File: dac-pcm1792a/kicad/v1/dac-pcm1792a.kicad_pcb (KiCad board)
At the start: 2 copper layers, 76.2 x 53.3 mm, 81 parts, among them IC1 PCM1702P, IC2 PCM1702P, J10 GND, J11 +15VAIN, J12 GND, J13 -15VAIN, J15 A, J16 +5VIN, J17 GND, J18 GND, J2 Conn_02x07_Odd_Even, J3 +5VAIN, J6 OUT, J7 -5VAIN, J8 GND, J9 OUT, U1 OPA1612, U2 TC1185-1.8VCT713, U3 TC1185-3.3VCT713, U4 XC2C64A-xVQ44, U5 CM1293A−04SO, U6 OPA1612

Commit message: WIP
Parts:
- removed C25: 10uF/10V, Capacitor_Tantalum_SMD:CP_EIA-3216-18_Kemet-A_Pad1.58x1.35mm_HandSolder
- removed C26: 100nF, Capacitor_SMD:C_0603_1608Metric_Pad1.08x0.95mm_HandSolder
- removed C27, C28, C29, C30: 10uF/25V, Capacitor_Tantalum_SMD:CP_EIA-3216-18_Kemet-A_Pad1.58x1.35mm_HandSolder
- removed C31, C42: 2n2, Capacitor_SMD:C_0805_2012Metric_Pad1.18x1.45mm_HandSolder
- removed C32, C43: 560p, Capacitor_SMD:C_0805_2012Metric_Pad1.18x1.45mm_HandSolder
- removed C41: 220pF, Capacitor_SMD:C_0805_2012Metric_Pad1.18x1.45mm_HandSolder
- removed IC1, IC2: PCM1702P, Package_DIP:DIP-16_W7.62mm
- removed J12, J8: GND, Connector_Pin:Pin_D1.0mm_L10.0mm
- removed J6: OUT, Connector_Pin:Pin_D1.0mm_L10.0mm
- removed J7: -5VAIN, Connector_Pin:Pin_D1.0mm_L10.0mm
- removed U1: OPA1612, Package_SO:SOIC-8_3.9x4.9mm_P1.27mm
- added J1: PORTB, Connector_PinHeader_2.54mm:PinHeader_1x08_P2.54mm_Vertical, F.Cu at (119.4, 97.8)
- added J4: GND, Connector_Pin:Pin_D1.0mm_L10.0mm, F.Cu at (161.3, 50.0)
- added J5: +5VAGND, Connector_Pin:Pin_D1.0mm_L10.0mm, F.Cu at (147.3, 111.1)
- added R1: 4k7, Resistor_SMD:R_0603_1608Metric_Pad0.98x0.95mm_HandSolder, F.Cu at (157.1, 49.8)
- added R12: 560R/0.1%, Resistor_SMD:R_0603_1608Metric_Pad0.98x0.95mm_HandSolder, F.Cu at (156.7, 83.8)
- added R13: 560R/0.1%, Resistor_SMD:R_0603_1608Metric_Pad0.98x0.95mm_HandSolder, F.Cu at (156.7, 81.3)
- added R14: 270R/0.1%, Resistor_SMD:R_0603_1608Metric_Pad0.98x0.95mm_HandSolder, F.Cu at (122.7, 34.9)
- added R15: 270R/0.1%, Resistor_SMD:R_0603_1608Metric_Pad0.98x0.95mm_HandSolder, F.Cu at (127.5, 31.9)
- added R16: 270R/0.1%, Resistor_SMD:R_0603_1608Metric_Pad0.98x0.95mm_HandSolder, F.Cu at (122.7, 37.4)
- added R17: 270R/0.1%, Resistor_SMD:R_0603_1608Metric_Pad0.98x0.95mm_HandSolder, F.Cu at (127.0, 34.9)
- added R18: 100R/0.1%, Resistor_SMD:R_0603_1608Metric_Pad0.98x0.95mm_HandSolder, F.Cu at (147.8, 52.9)
- added R19: 100R/0.1%, Resistor_SMD:R_0603_1608Metric_Pad0.98x0.95mm_HandSolder, F.Cu at (152.6, 50.0)
- added R2: 10k, Resistor_SMD:R_0603_1608Metric_Pad0.98x0.95mm_HandSolder, F.Cu at (150.3, 55.7)
- added R3: 33R, Resistor_SMD:R_0603_1608Metric_Pad0.98x0.95mm_HandSolder, F.Cu at (164.4, 42.4)
- C1: value 220pF -> 10uF/10V; footprint Capacitor_SMD:C_0805_2012Metric_Pad1.18x1.45mm_HandSolder -> Capacitor_Tantalum_SMD:CP_EIA-3216-18_Kemet-A_Pad1.58x1.35mm_HandSolder; moved to B.Cu
- C10: value 100uF -> 10uF/10V; footprint Capacitor_SMD:C_1206_3216Metric_Pad1.33x1.80mm_HandSolder -> Capacitor_Tantalum_SMD:CP_EIA-3216-18_Kemet-A_Pad1.58x1.35mm_HandSolder; moved to B.Cu
- C11, C12: value 100uF -> 47uF/10V; footprint Capacitor_SMD:C_1206_3216Metric_Pad1.33x1.80mm_HandSolder -> Capacitor_Tantalum_SMD:CP_EIA-3528-12_Kemet-T_Pad1.50x2.35mm_HandSolder; moved to B.Cu
- C13, C14, C15: value 100nF -> 2200pF/2%; footprint Capacitor_SMD:C_0603_1608Metric_Pad1.08x0.95mm_HandSolder -> Capacitor_SMD:C_0805_2012Metric_Pad1.18x1.45mm_HandSolder
- C16: value 10uF/25V -> 2200pF/2%; footprint Capacitor_Tantalum_SMD:CP_EIA-3216-18_Kemet-A_Pad1.58x1.35mm_HandSolder -> Capacitor_SMD:C_0805_2012Metric_Pad1.18x1.45mm_HandSolder
- C17: value 10uF/25V -> 2700pF/2%; footprint Capacitor_Tantalum_SMD:CP_EIA-3216-18_Kemet-A_Pad1.58x1.35mm_HandSolder -> Capacitor_SMD:C_0805_2012Metric_Pad1.18x1.45mm_HandSolder
- C18: value 10uF/10V -> 2700pF/2%; footprint Capacitor_Tantalum_SMD:CP_EIA-3216-18_Kemet-A_Pad1.58x1.35mm_HandSolder -> Capacitor_SMD:C_0805_2012Metric_Pad1.18x1.45mm_HandSolder
- C19, C20: value 100uF -> 2700pF/2%; footprint Capacitor_SMD:C_1206_3216Metric_Pad1.33x1.80mm_HandSolder -> Capacitor_SMD:C_0805_2012Metric_Pad1.18x1.45mm_HandSolder
- C21: value 100uF -> 10uF/25V; footprint Capacitor_SMD:C_1206_3216Metric_Pad1.33x1.80mm_HandSolder -> Capacitor_Tantalum_SMD:CP_EIA-3528-21_Kemet-B_Pad1.50x2.35mm_HandSolder
- C22: value 100nF -> 10uF/25V; footprint Capacitor_SMD:C_0603_1608Metric_Pad1.08x0.95mm_HandSolder -> Capacitor_Tantalum_SMD:CP_EIA-3528-21_Kemet-B_Pad1.50x2.35mm_HandSolder
- C3: value 10uF -> 10uF/10V; footprint Capacitor_SMD:C_0805_2012Metric_Pad1.18x1.45mm_HandSolder -> Capacitor_Tantalum_SMD:CP_EIA-3216-18_Kemet-A_Pad1.58x1.35mm_HandSolder; moved to B.Cu
- C8: moved to B.Cu
- C9: value 100nF -> 10uF/10V; footprint Capacitor_SMD:C_0603_1608Metric_Pad1.08x0.95mm_HandSolder -> Capacitor_Tantalum_SMD:CP_EIA-3216-18_Kemet-A_Pad1.58x1.35mm_HandSolder
- J2: value Conn_02x07_Odd_Even -> OUT; footprint Connector_PinHeader_2.00mm:PinHeader_2x07_P2.00mm_Vertical -> Connector_Pin:Pin_D1.0mm_L10.0mm
- R10: value 4.7k -> 560R/0.1%; footprint Resistor_SMD:R_0805_2012Metric_Pad1.20x1.40mm_HandSolder -> Resistor_SMD:R_0603_1608Metric_Pad0.98x0.95mm_HandSolder
- R11: value 2k -> 560R/0.1%; footprint Resistor_SMD:R_0805_2012Metric_Pad1.20x1.40mm_HandSolder -> Resistor_SMD:R_0603_1608Metric_Pad0.98x0.95mm_HandSolder
- R4: value 2.5k -> 33R; footprint Resistor_SMD:R_0805_2012Metric_Pad1.20x1.40mm_HandSolder -> Resistor_SMD:R_0603_1608Metric_Pad0.98x0.95mm_HandSolder
- R5: value 4.7k -> 33R; footprint Resistor_SMD:R_0805_2012Metric_Pad1.20x1.40mm_HandSolder -> Resistor_SMD:R_0603_1608Metric_Pad0.98x0.95mm_HandSolder
- R6, R9: value 4.7k -> 750R/0.1%; footprint Resistor_SMD:R_0805_2012Metric_Pad1.20x1.40mm_HandSolder -> Resistor_SMD:R_0603_1608Metric_Pad0.98x0.95mm_HandSolder
- R7: value 2k -> 750R/0.1%; footprint Resistor_SMD:R_0805_2012Metric_Pad1.20x1.40mm_HandSolder -> Resistor_SMD:R_0603_1608Metric_Pad0.98x0.95mm_HandSolder
- R8: value 2.5k -> 750R/0.1%; footprint Resistor_SMD:R_0805_2012Metric_Pad1.20x1.40mm_HandSolder -> Resistor_SMD:R_0603_1608Metric_Pad0.98x0.95mm_HandSolder
- U2: value TC1185-1.8VCT713 -> PCM1792A; footprint Package_TO_SOT_SMD:SOT-23-5 -> Package_SO:SSOP-28_5.3x10.2mm_P0.65mm
- U4: value XC2C64A-xVQ44 -> OPA1612; footprint Package_QFP:TQFP-44_10x10mm_P0.8mm -> Package_SO:SOIC-8_3.9x4.9mm_P1.27mm
- U5: value CM1293A−04SO -> OPA1612; footprint Package_SO:SC-74-6_1.5x2.9mm_P0.95mm -> Package_SO:SOIC-8_3.9x4.9mm_P1.27mm
- moved C19 79.1 mm to (122.9, 32.1)
- moved C20 67.4 mm to (118.1, 38.1)
- moved U5 67.1 mm to (174.6, 54.0)
- moved J2 55.1 mm to (154.5, 56.0)
- moved C17 50.1 mm to (118.1, 32.1), turned to 0 degrees
- moved C13 41.8 mm to (151.6, 107.5), turned to 0 degrees
- moved C18 41.2 mm to (118.1, 35.1), turned to 0 degrees
- moved R6 36.2 mm to (151.5, 105.5), turned to 0 degrees
- moved R7 31.0 mm to (152.1, 95.6), turned to 0 degrees
- moved C37 30.7 mm to (146.4, 76.1)
- moved C1 30.5 mm to (137.2, 83.8), turned to 180 degrees
- moved U4 29.3 mm to (152.4, 100.3)
- moved C12 28.6 mm to (137.2, 88.9)
- moved R5 27.9 mm to (163.0, 44.9), turned to 0 degrees
- moved C14 25.3 mm to (152.1, 93.8), turned to 0 degrees
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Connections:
- C1 pad 1: Net-(C1-Pad1) -> +5VA
- C1 pad 2: Net-(C1-Pad2) -> GND
- C10 pad 1: Net-(C10-Pad1) -> +5VA
- C11 pad 1: Net-(C11-Pad1) -> +5VA
- C11 pad 2: -5VA -> Net-(C11-Pad2)
- C12 pad 1: Net-(C12-Pad1) -> +5VA
- C12 pad 2: -5VA -> Net-(C12-Pad2)
- C13 pad 1: -5VA -> Net-(C13-Pad1)
- C13 pad 2: GND -> Net-(C13-Pad2)
- C14 pad 1: +5VA -> Net-(C14-Pad1)
- C14 pad 2: GND -> Net-(C14-Pad2)
- C15 pad 1: -5VA -> Net-(C15-Pad1)
- C15 pad 2: GND -> Net-(C15-Pad2)
- C16 pad 1: +5VA -> Net-(C16-Pad1)
- C16 pad 2: GND -> Net-(C16-Pad2)
- C17 pad 2: -5VA -> Net-(C17-Pad2)
- C18 pad 1: +5VA -> Net-(C18-Pad1)
- C18 pad 2: GND -> Net-(C18-Pad2)
- C19 pad 1: Net-(C19-Pad1) -> GND
- C19 pad 2: GND -> Net-(C19-Pad2)
- C20 pad 2: -5VA -> Net-(C20-Pad2)
- C21 pad 1: Net-(C21-Pad1) -> +15V
- C21 pad 2: -5VA -> GND
- C22 pad 1: -5VA -> GND
- C22 pad 2: GND -> -15V
- C23 pad 1: +5VA -> +15V
- C24 pad 1: -5VA -> GND
- C24 pad 2: GND -> -15V
- C3 pad 1: +1V8 -> +3V3
- C5 pad 1: GND -> +5VA
- C5 pad 2: +3V3 -> GND
- C6 pad 1: GND -> +3V3
- C6 pad 2: +3V3 -> GND
- C7 pad 1: GND -> +5VA
- C7 pad 2: +1V8 -> GND
- C8 pad 1: GND -> +5VA
- C8 pad 2: +3V3 -> GND
- J15 pad 10: (no net) -> Net-(J1-Pad7)
- J15 pad 6: (no net) -> Net-(J1-Pad5)
- J15 pad 8: (no net) -> Net-(J1-Pad6)
- J2 pad 1: GND -> Net-(J2-Pad1)
- J9 pad 1: Net-(C43-Pad1) -> Net-(J9-Pad1)
- R10 pad 1: Net-(C31-Pad1) -> Net-(C17-Pad2)
- R10 pad 2: Net-(C32-Pad1) -> Net-(C13-Pad1)
- R11 pad 1: Net-(C32-Pad2) -> Net-(C18-Pad1)
- R11 pad 2: Net-(C31-Pad1) -> Net-(C14-Pad1)
- R4 pad 1: Net-(C41-Pad2) -> SCL
- R4 pad 2: Net-(C41-Pad1) -> Net-(J1-Pad6)
- R5 pad 1: Net-(C42-Pad1) -> SDA
- R5 pad 2: Net-(C41-Pad2) -> Net-(J1-Pad5)
- R6 pad 1: Net-(C42-Pad1) -> Net-(C13-Pad1)
- R6 pad 2: Net-(C43-Pad1) -> Net-(C13-Pad2)
- R7 pad 1: Net-(C43-Pad2) -> Net-(C14-Pad1)
- R7 pad 2: Net-(C42-Pad1) -> Net-(C14-Pad2)
- R8 pad 1: Net-(C1-Pad2) -> Net-(C15-Pad1)
- R8 pad 2: Net-(C1-Pad1) -> Net-(C15-Pad2)
- R9 pad 1: Net-(C31-Pad1) -> Net-(C16-Pad1)
- R9 pad 2: Net-(C1-Pad2) -> Net-(C16-Pad2)
- U2 pad 1: Net-(C2-Pad1) -> (no net)
- U2 pad 2: GND -> (no net)
- U2 pad 3: Net-(C2-Pad1) -> Net-(R1-Pad2)
- U2 pad 4: (no net) -> LRCK
- U2 pad 5: +1V8 -> DATAIN
- U4 pad 1: (no net) -> Net-(C13-Pad1)
- U4 pad 2: (no net) -> Net-(C13-Pad2)
- U4 pad 3: (no net) -> GND
- U4 pad 4: GND -> -15V
- U4 pad 5: (no net) -> GND
- U4 pad 6: (no net) -> Net-(C14-Pad2)
- U4 pad 7: +3V3 -> Net-(C14-Pad1)
- U4 pad 8: (no net) -> +15V
- U5 pad 1: JTAG_TMS -> Net-(C20-Pad2)
- U5 pad 2: GND -> Net-(C20-Pad1)
- U5 pad 3: JTAG_TDO -> Net-(C19-Pad2)
- U5 pad 4: JTAG_TCK -> -15V
- U5 pad 5: +3V3 -> Net-(C17-Pad2)
- U5 pad 6: JTAG_TDI -> Net-(C18-Pad1)
- U6 pad 1: Net-(C41-Pad2) -> Net-(C15-Pad1)
- U6 pad 2: Net-(C41-Pad1) -> Net-(C15-Pad2)
- U6 pad 6: Net-(C43-Pad2) -> Net-(C16-Pad2)
- U6 pad 7: Net-(C43-Pad1) -> Net-(C16-Pad1)
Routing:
- net -5VA: track 105.7 -> 0.00 mm, vias 3 -> 0
- net +5VA: track 77.8 -> 0.00 mm, vias 3 -> 0
- net +3V3: track 74.6 -> 0.01 mm, vias 5 -> 0
- net +15V: track 45.2 -> 0.00 mm, vias 2 -> 0
- net JTAG_TDO: track 44.7 -> 0.00 mm, vias 4 -> 0
- net -15V: track 41.9 -> 0.00 mm, vias 2 -> 0
- net JTAG_TDI: track 33.7 -> 0.00 mm, vias 6 -> 0
- net JTAG_TCK: track 32.0 -> 0.00 mm, vias 4 -> 0
- net +1V8: track 29.6 -> 0.00 mm, vias 2 -> 0
- net JTAG_TMS: track 28.1 -> 0.00 mm, vias 4 -> 0
- net Net-(C2-Pad1): track 22.5 -> 0.00 mm, vias 3 -> 0
- net LEOUTL: track 21.8 -> 0.00 mm, vias 1 -> 0
- net Net-(C32-Pad1): track 16.9 -> 0.00 mm, vias 2 -> 0
- net Net-(C43-Pad1): track 16.7 -> 0.00 mm, vias 2 -> 0
- net DATAOUTR: track 16.0 -> 0.00 mm, vias 1 -> 0
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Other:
- board text added: "DAC PCM1792A V1 Michael Schenk 2021.06.06"
- board text removed: "-5VA"
- board text removed: "I2S NOS CPLD V4 Michael Schenk 2021.05.14"
- board text removed: "JTAG"

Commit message: WIP
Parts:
- C3: moved to F.Cu
- moved R3 55.7 mm to (123.3, 80.1), turned to 180 degrees
- moved R5 55.1 mm to (123.3, 83.2), turned to 180 degrees
- moved R4 35.8 mm to (123.3, 81.7), turned to 180 degrees
- moved U5 31.5 mm to (173.5, 85.5)
- moved R24 13.0 mm to (123.3, 97.8)
- moved R25 12.1 mm to (123.3, 95.2)
- moved R26 11.2 mm to (123.3, 92.7)
- moved R27 10.3 mm to (123.3, 90.2)
- moved R12 8.46 mm to (158.6, 75.5)
- moved R13 8.46 mm to (158.6, 73.1)
- moved C16 8.46 mm to (153.6, 67.9)
- moved C38 8.46 mm to (159.2, 79.5)
- moved R8 8.46 mm to (152.2, 78.8)
- moved R9 8.46 mm to (153.6, 69.8)
- moved U6 8.46 mm to (153.6, 74.3)
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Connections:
- J1 pad 1: (no net) -> Net-(J1-Pad1)
- J1 pad 2: (no net) -> Net-(J1-Pad2)
- J1 pad 3: (no net) -> Net-(J1-Pad3)
- J1 pad 4: (no net) -> Net-(J1-Pad4)
- J15 pad 1: Net-(J15-Pad1) -> Net-(J1-Pad1)
- J15 pad 3: Net-(J15-Pad3) -> Net-(J1-Pad2)
- J15 pad 5: Net-(J15-Pad5) -> Net-(J1-Pad3)
- J15 pad 7: Net-(J15-Pad7) -> Net-(J1-Pad4)
- R24 pad 1: Net-(J15-Pad1) -> Net-(J1-Pad1)
- R25 pad 1: Net-(J15-Pad3) -> Net-(J1-Pad2)
- R26 pad 1: Net-(J15-Pad5) -> Net-(J1-Pad3)
- R27 pad 1: Net-(J15-Pad7) -> Net-(J1-Pad4)
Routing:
- net Net-(J1-Pad1): track 0.00 -> 8.32 mm
- net Net-(J1-Pad3): track 0.00 -> 8.32 mm
- net Net-(J1-Pad2): track 0.00 -> 8.32 mm
- net Net-(J1-Pad4): track 0.00 -> 8.26 mm
- net Net-(J1-Pad7): track 0.00 -> 6.76 mm
- net Net-(J1-Pad5): track 0.00 -> 6.76 mm
- net Net-(J1-Pad6): track 0.00 -> 6.76 mm
- net SDA: track 0.00 -> 1.83 mm, vias 0 -> 1
- net +5VA: track 0.00 -> 1.56 mm, vias 0 -> 1
- net RESET: track 0.00 -> 1.45 mm, vias 0 -> 1
- net SCL: track 0.00 -> 1.34 mm, vias 0 -> 1
- net LRCK: track 0.54 -> 0.00 mm

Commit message: Update dac-pcm1792a.kicad_pcb
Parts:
- moved C6 1.27 mm to (130.9, 88.8), turned to 270 degrees
- moved C3 1.01 mm to (129.0, 89.4), turned to 270 degrees
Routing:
- net RESET: track 1.45 -> 22.2 mm, vias 1 -> 2
- net SCL: track 1.34 -> 18.9 mm, vias 1 -> 2
- net SDA: track 1.83 -> 18.0 mm, vias 1 -> 2
- net LRCK: track 0.00 -> 13.5 mm, vias 0 -> 2
- net DATAIN: track 0.00 -> 10.7 mm, vias 0 -> 2
- net GND: track 1.20 -> 9.52 mm
- net Net-(J1-Pad5): track 6.76 -> 12.6 mm, vias 0 -> 1
- net Net-(J1-Pad6): track 6.76 -> 12.0 mm, vias 0 -> 1
- net Net-(J1-Pad7): track 6.76 -> 11.0 mm, vias 0 -> 1
- net +3V3: track 0.01 -> 3.91 mm, vias 0 -> 1
- net MCLK: track 0.00 -> 1.84 mm, vias 0 -> 1
- net BCK: track 0.00 -> 1.43 mm, vias 0 -> 1

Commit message: WIP
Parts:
- moved R1 43.1 mm to (129.9, 83.1), turned to 270 degrees
- moved C2 5.55 mm to (131.2, 106.1), turned to 0 degrees
- moved U3 4.80 mm to (131.1, 103.0)
- moved R24 4.70 mm to (123.3, 93.1)
- moved R25 4.32 mm to (123.3, 90.9)
- moved C4 4.18 mm to (131.2, 100.0)
- moved R26 3.30 mm to (123.3, 89.4)
- moved R27 2.86 mm to (123.3, 87.3)
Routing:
- net +3V3: track 3.91 -> 17.9 mm, vias 1 -> 2
- net Net-(C2-Pad1): track 0.00 -> 11.5 mm, vias 0 -> 1
- net MCLK: track 1.84 -> 12.0 mm, vias 1 -> 2
- net BCK: track 1.43 -> 10.8 mm, vias 1 -> 2
- net Net-(J1-Pad1): track 8.32 -> 5.27 mm
- net Net-(J1-Pad3): track 8.32 -> 5.27 mm
- net Net-(J1-Pad2): track 8.32 -> 5.27 mm
- net Net-(J1-Pad4): track 8.26 -> 5.27 mm
- net LRCK: track 13.5 -> 11.9 mm
- net GND: track 9.52 -> 10.7 mm
- net DATAIN: track 10.7 -> 9.56 mm

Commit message: WIP
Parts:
- C10, C8: moved to F.Cu
- moved C18 78.0 mm to (168.6, 94.6)
- moved C17 75.8 mm to (164.7, 91.8), turned to 90 degrees
- moved R15 73.5 mm to (168.6, 92.8)
- moved R14 69.6 mm to (162.9, 91.7), turned to 90 degrees
- moved C20 69.2 mm to (171.4, 82.4)
- moved C19 65.9 mm to (168.9, 79.4), turned to 270 degrees
- moved R17 63.4 mm to (172.3, 79.2)
- moved R16 61.0 mm to (166.9, 79.3), turned to 270 degrees
- moved J4 50.9 mm to (181.4, 96.8)
- moved R18 45.1 mm to (174.7, 89.2), turned to 180 degrees
- moved J2 43.9 mm to (181.4, 90.7)
- moved R19 43.4 mm to (174.7, 87.4), turned to 180 degrees
- moved R2 33.1 mm to (143.1, 87.9), turned to 180 degrees
- moved J3 17.7 mm to (136.2, 111.5)
- moved C36 17.7 mm to (162.4, 84.2), turned to 270 degrees
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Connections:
- U4 pad 1: Net-(C13-Pad1) -> Net-(C14-Pad1)
- U4 pad 2: Net-(C13-Pad2) -> Net-(C14-Pad2)
- U4 pad 6: Net-(C14-Pad2) -> Net-(C13-Pad2)
- U4 pad 7: Net-(C14-Pad1) -> Net-(C13-Pad1)
- U6 pad 1: Net-(C15-Pad1) -> Net-(C16-Pad1)
- U6 pad 2: Net-(C15-Pad2) -> Net-(C16-Pad2)
- U6 pad 6: Net-(C16-Pad2) -> Net-(C15-Pad2)
- U6 pad 7: Net-(C16-Pad1) -> Net-(C15-Pad1)
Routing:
- net +5VA: track 1.56 -> 61.2 mm, vias 1 -> 4
- net -15V: track 0.00 -> 34.4 mm, vias 0 -> 3
- net +15V: track 0.00 -> 32.8 mm, vias 0 -> 2
- net GND: track 10.7 -> 32.9 mm, vias 0 -> 1
- net Net-(C15-Pad2): track 0.00 -> 20.8 mm, vias 0 -> 2
- net Net-(C14-Pad2): track 0.00 -> 20.7 mm, vias 0 -> 2
- net Net-(C13-Pad2): track 0.00 -> 20.2 mm, vias 0 -> 2
- net Net-(C16-Pad2): track 0.00 -> 18.3 mm, vias 0 -> 2
- net Net-(C14-Pad1): track 0.00 -> 11.0 mm
- net Net-(C16-Pad1): track 0.00 -> 11.0 mm
- net +3V3: track 17.9 -> 7.10 mm
- net Net-(C13-Pad1): track 0.00 -> 10.3 mm
- net Net-(C18-Pad2): track 0.00 -> 9.85 mm
- net Net-(C15-Pad1): track 0.00 -> 9.85 mm
- net Net-(C12-Pad2): track 0.00 -> 4.51 mm, vias 0 -> 1
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
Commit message: WIP
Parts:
- moved R17 5.09 mm to (170.1, 83.8)
- moved R16 3.87 mm to (165.2, 82.8)
- moved C19 3.76 mm to (167.1, 82.7)
- moved C34 1.75 mm to (165.0, 86.8), turned to 90 degrees
- moved C20 1.24 mm to (170.2, 82.0)
- moved C18 0.38 mm to (168.9, 94.6)
- moved R15 0.23 mm to (168.8, 92.8)
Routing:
- net Net-(C20-Pad1): track 0.00 -> 17.0 mm, vias 0 -> 2
- net Net-(C19-Pad2): track 0.00 -> 14.1 mm, vias 0 -> 2
- net Net-(C17-Pad2): track 0.00 -> 11.2 mm, vias 0 -> 2
- net Net-(C18-Pad1): track 3.97 -> 14.4 mm, vias 0 -> 2
- net Net-(C20-Pad2): track 4.00 -> 8.20 mm

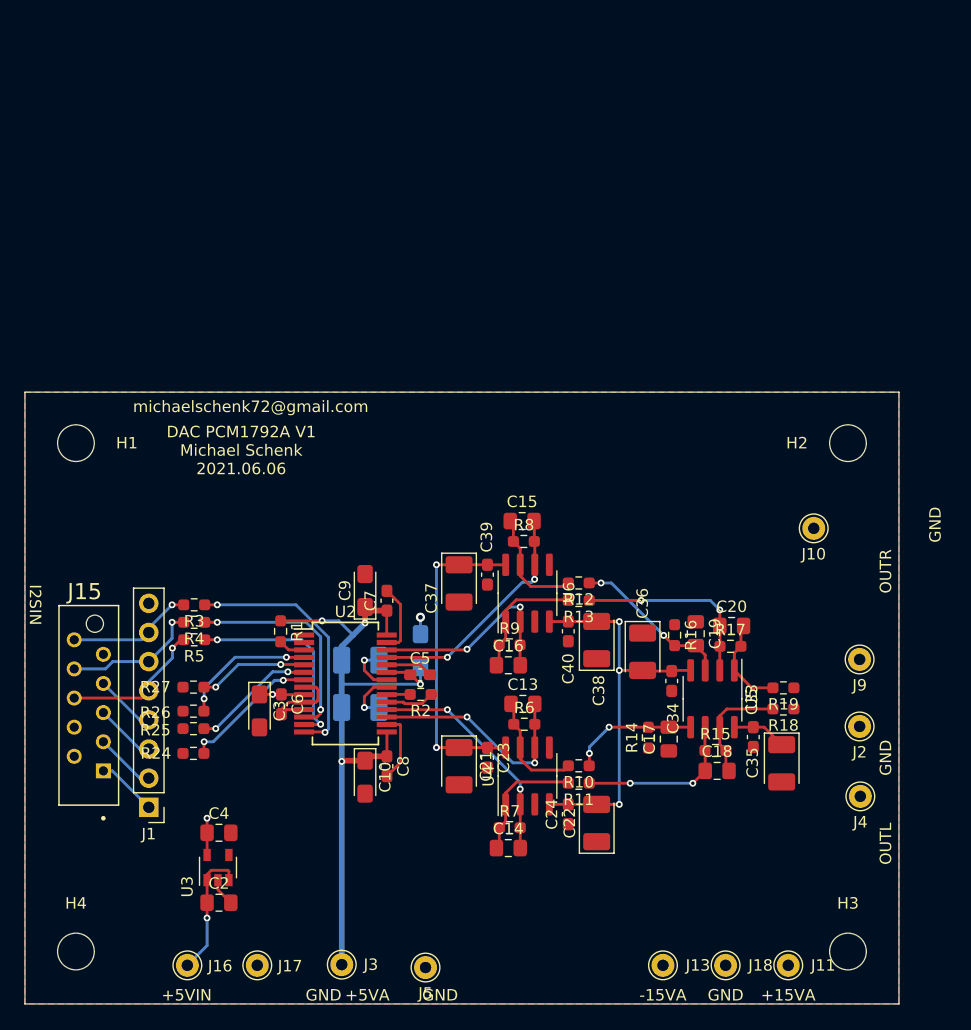
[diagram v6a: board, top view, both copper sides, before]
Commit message: first drop layout complete
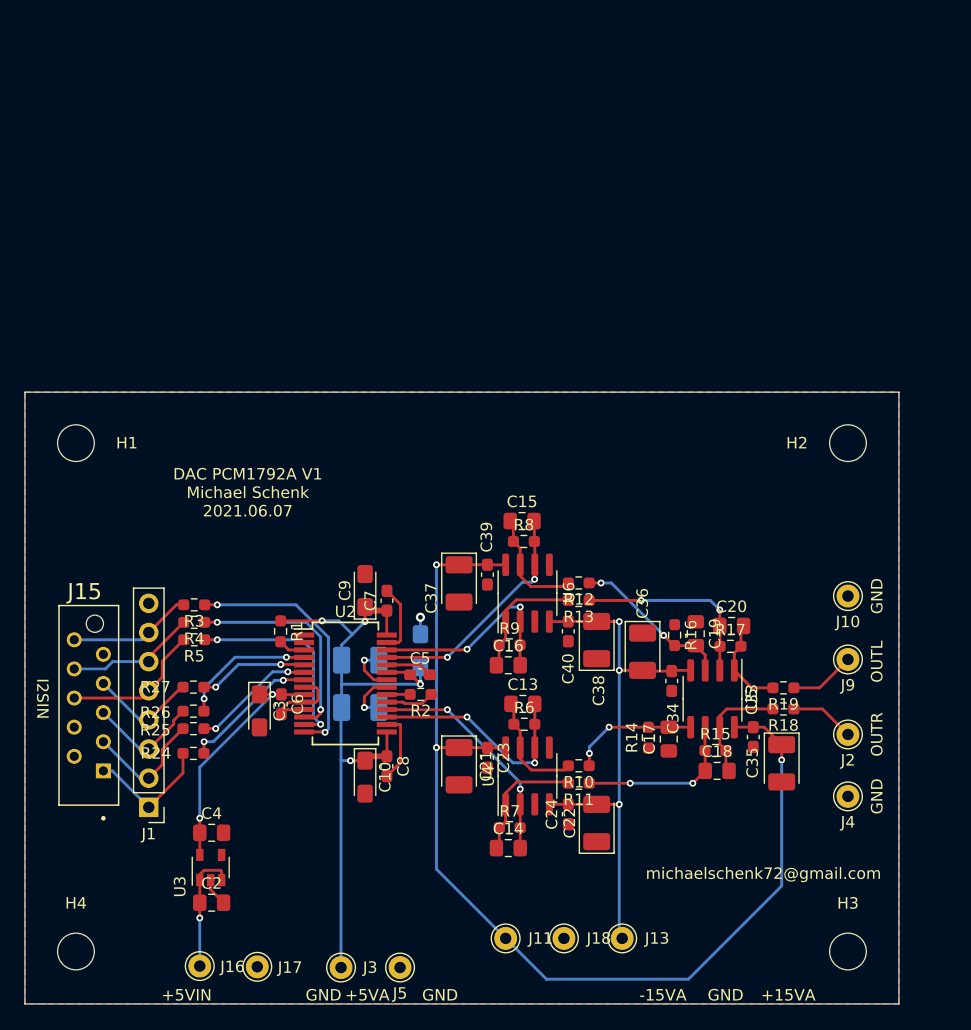
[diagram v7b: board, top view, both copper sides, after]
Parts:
- J1: value PORTB -> DEBUG
- J10: value GND -> GNDL
- J2: value OUT -> OUTR
- J4: value GND -> GNDR
- J9: value OUT -> OUTL
- moved J11 24.7 mm to (150.5, 109.2)
- moved J18 14.3 mm to (155.6, 109.2)
- moved J10 6.62 mm to (180.3, 79.4)
- moved J13 4.26 mm to (160.7, 109.2)
- moved J5 2.22 mm to (141.3, 111.8)
- moved J2 1.23 mm to (180.3, 91.4)
- moved J16 1.08 mm to (123.8, 111.6)
- moved J4 1.08 mm to (180.3, 96.8)
- moved J9 1.02 mm to (180.3, 84.9)
- moved C2 0.64 mm to (124.9, 106.1)
- moved C4 0.64 mm to (124.9, 100.0)
- moved U3 0.64 mm to (124.8, 103.0)
- moved J3 0.26 mm to (136.1, 111.8)
- moved J17 0.13 mm to (128.8, 111.7)
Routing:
- net +15V: track 32.8 -> 93.1 mm, vias 2 -> 3
- net +3V3: track 7.10 -> 20.5 mm
- net -15V: track 34.5 -> 46.3 mm
- net Net-(J1-Pad1): track 5.27 -> 11.2 mm
- net Net-(J9-Pad1): track 0.00 -> 5.74 mm
- net Net-(J2-Pad1): track 0.00 -> 5.64 mm
- net Net-(J1-Pad2): track 5.27 -> 10.8 mm
- net Net-(J1-Pad3): track 5.27 -> 9.81 mm
- net Net-(J1-Pad4): track 5.27 -> 9.44 mm
- net Net-(C2-Pad1): track 11.5 -> 10.8 mm
- net Net-(J1-Pad6): track 12.0 -> 11.5 mm, vias 1 -> 0
- net Net-(J1-Pad7): track 11.0 -> 10.8 mm, vias 1 -> 0
- net Net-(J1-Pad5): track 12.6 -> 12.7 mm, vias 1 -> 0
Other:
- board text added: "DAC PCM1792A V1 Michael Schenk 2021.06.07"
- board text removed: "DAC PCM1792A V1 Michael Schenk 2021.06.06"
